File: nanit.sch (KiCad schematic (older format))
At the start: 66 parts, among them J1 USB_B_Micro, J2 Nokia 2660/2760 mini, Q1 BC857, Q2 IRLML6344, Q4 BC847, SW1 Button 1, SW2 Button 2, U1 LTC4054ES5-4.2, U2 ATmega88PA-AU, Y1 32.768 KHz

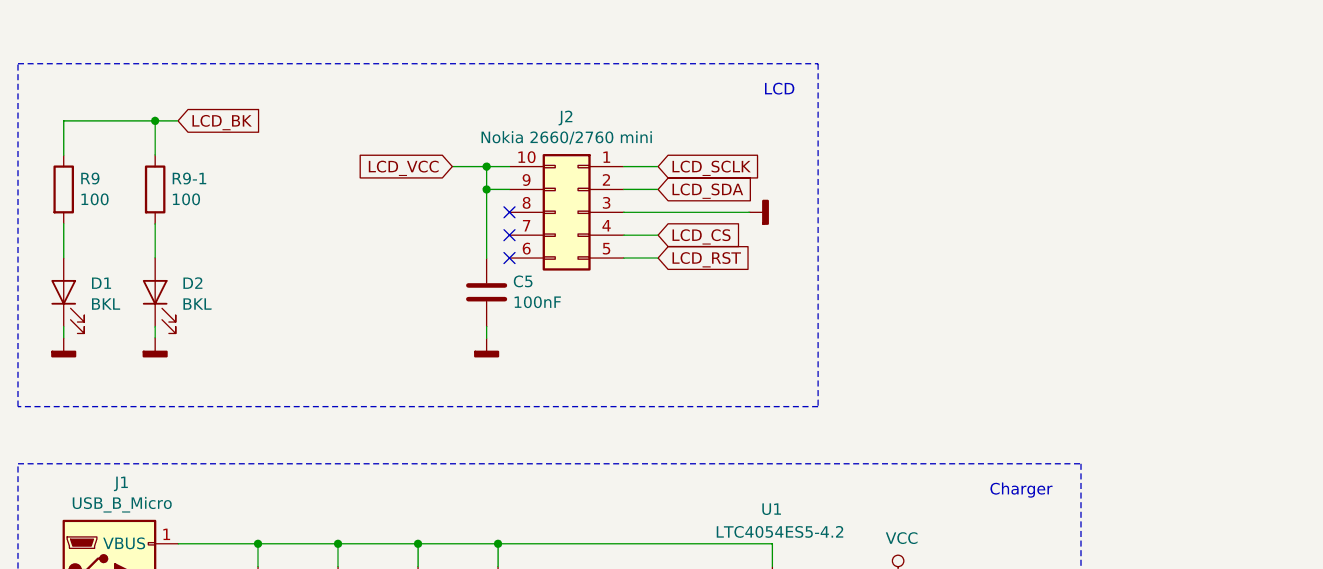
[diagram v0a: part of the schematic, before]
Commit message: Added LED driver for LCD display, gerbers for rev.A
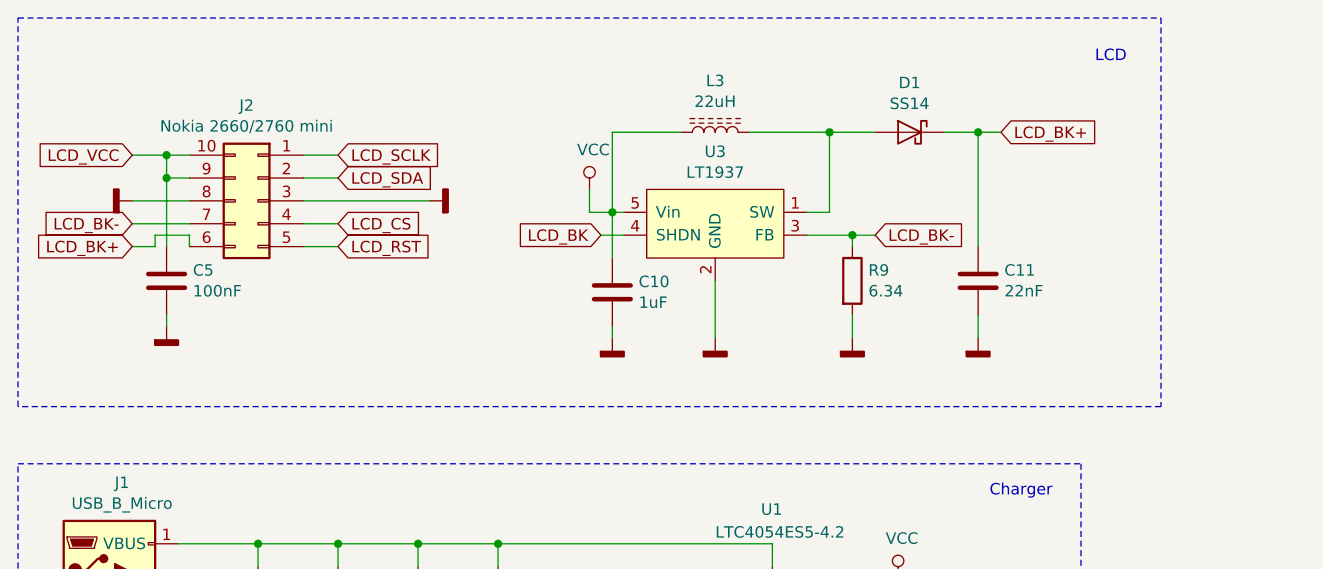
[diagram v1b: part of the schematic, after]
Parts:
- removed D1, D2: BKL, LED_SMD:LED_1206_3216Metric_Pad1.42x1.75mm_HandSolder, symbol Device:LED
- removed R9-1: 100, Resistor_SMD:R_0805_2012Metric_Pad1.15x1.40mm_HandSolder, symbol Device:R
- added C10: 1uF, Capacitor_SMD:C_0805_2012Metric_Pad1.15x1.40mm_HandSolder, symbol Device:C
- added C11: 22nF, Capacitor_SMD:C_0805_2012Metric_Pad1.15x1.40mm_HandSolder, symbol Device:C
- added D1: SS14, Diode_SMD:D_SMA, symbol Device:D_Schottky
- added L3: 22uH, Inductor_SMD:L_Bourns-SRN6028, symbol Device:L_Core_Ferrite
- added U3: LT1937, Package_TO_SOT_SMD:SOT-23-5_HandSoldering, symbol doz:LT1937
- R9: value 100 -> 6.34
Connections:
- net GNDD: now also J2.8 (Pin_8), R9.2, C10.2, C11.2, U3.2 (GND)
- net LCD_BK: now also U3.4 (SHDN); no longer R9.1
- net VCC: now also C10.1, L3.1, U3.5 (Vin)
- net LCD_BK+: now reaches J2.6 (Pin_6)
- net LCD_BK+: now also C11.1, D1.1 (K)
- net LCD_BK-: now reaches J2.7 (Pin_7)
- net LCD_BK-: now also R9.1, U3.3 (FB)
- new net: D1.2 (A), L3.2, U3.1 (SW)
- no-connect marks 15 -> 12
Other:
- moved on the sheet: C5, J2
